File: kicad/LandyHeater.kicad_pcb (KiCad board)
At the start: 4 copper layers, 0 parts

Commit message: Place Rev B board: outline, zoned placement, mounting holes, V-01 transient check
- 80 x 50 mm outline, all 131 parts on the top side, 4 x M3 board-only holes
- Custom DRC rules: 0.2 mm general clearance with justified exceptions for
  fine-pitch IC pads, the USB pair and the USB-C guide pins; 0.2 mm min drill
- ngspice transient check of the 12 V input (ISO 7637-2 level IV pulses)
- Phase 3 report for approval

Co-Authored-By: Claude Opus 5.5 <noreply@anthropic.com>
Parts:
- added BT1: BR1225, LandyHeater:BatteryClip_MYOUNG_MY-1225-01-J, F.Cu at (129.0, 108.0)
- added C1: 47uF, Capacitor_SMD:CP_Elec_6.3x7.7, F.Cu at (117.7, 132.0)
- added C10: 22uF, Capacitor_SMD:C_1206_3216Metric, F.Cu at (120.0, 119.5)
- added C11: 22uF, Capacitor_SMD:C_1206_3216Metric, F.Cu at (120.0, 124.2)
- added C12: 22uF, Capacitor_SMD:C_1206_3216Metric, F.Cu at (147.6, 102.9)
- added C13: 22uF, Capacitor_SMD:C_1206_3216Metric, F.Cu at (150.3, 102.9)
- added C14: 100nF, Capacitor_SMD:C_0603_1608Metric, F.Cu at (147.2, 107.1)
- added C15: 1uF, Capacitor_SMD:C_0603_1608Metric, F.Cu at (145.3, 102.1)
- added C16: 100nF, Capacitor_SMD:C_0603_1608Metric, F.Cu at (149.8, 119.7)
- added C17: 10pF, Capacitor_SMD:C_0603_1608Metric, F.Cu at (153.0, 129.4)
- added C18: 10pF, Capacitor_SMD:C_0603_1608Metric, F.Cu at (166.1, 130.9)
- added C19: 100nF, Capacitor_SMD:C_0603_1608Metric, F.Cu at (131.0, 116.4)
- added C2: 1uF, Capacitor_SMD:C_0603_1608Metric, F.Cu at (160.6, 124.2)
- added C20: 1uF, Capacitor_SMD:C_0603_1608Metric, F.Cu at (129.3, 123.8)
- added C21: 100nF, Capacitor_SMD:C_0603_1608Metric, F.Cu at (126.4, 125.7)
- added C22: 100nF, Capacitor_SMD:C_0603_1608Metric, F.Cu at (123.0, 125.7)
- added C23: 1uF, Capacitor_SMD:C_0603_1608Metric, F.Cu at (149.6, 127.9)
- added C24: 1uF, Capacitor_SMD:C_0603_1608Metric, F.Cu at (142.0, 128.3)
- added C25: 10nF, Capacitor_SMD:C_0603_1608Metric, F.Cu at (134.1, 128.3)
- added C3: 10nF, Capacitor_SMD:C_0603_1608Metric, F.Cu at (166.3, 127.5)
- added C4: 1nF, Capacitor_SMD:C_0603_1608Metric, F.Cu at (154.9, 127.6)
- added C5: 4.7uF, Capacitor_SMD:C_0603_1608Metric, F.Cu at (156.8, 127.6)
- added C6: 4.7uF, Capacitor_SMD:C_1206_3216Metric, F.Cu at (104.5, 121.5)
- added C7: 100nF, Capacitor_SMD:C_0603_1608Metric, F.Cu at (107.0, 121.5)
- added C8: 1uF, Capacitor_SMD:C_0603_1608Metric, F.Cu at (110.0, 125.0)
- added C9: 100nF, Capacitor_SMD:C_0603_1608Metric, F.Cu at (113.5, 117.5)
- added D1: SMBJ18CA, Diode_SMD:D_SMB, F.Cu at (103.5, 131.5)
- added D10: PESD3V3S2UT, Package_TO_SOT_SMD:SOT-23, F.Cu at (135.3, 124.7)
- added D11: rot, LED_SMD:LED_0603_1608Metric, F.Cu at (109.2, 101.4)
- added D12: rot, LED_SMD:LED_0603_1608Metric, F.Cu at (112.6, 101.4)
- added D13: rot, LED_SMD:LED_0603_1608Metric, F.Cu at (116.0, 101.4)
- added D14: rot, LED_SMD:LED_0603_1608Metric, F.Cu at (112.6, 103.3)
- added D15: BAS116, Package_TO_SOT_SMD:SOT-23, F.Cu at (115.5, 108.2)
- added D16: BAS116, Package_TO_SOT_SMD:SOT-23, F.Cu at (109.7, 109.0)
- added D17: BAS116, Package_TO_SOT_SMD:SOT-23, F.Cu at (102.6, 109.4)
- added D18: BAS116, Package_TO_SOT_SMD:SOT-23, F.Cu at (114.0, 112.0)
- added D19: rot, LED_SMD:LED_0603_1608Metric, F.Cu at (109.2, 103.3)
- added D2: SS16, Diode_SMD:D_SMA, F.Cu at (108.5, 131.5)
- added D20: rot, LED_SMD:LED_0603_1608Metric, F.Cu at (145.9, 116.3)
- added D21: rot, LED_SMD:LED_0603_1608Metric, F.Cu at (147.8, 116.3)
- added D3: ESD5Z5.0, Diode_SMD:D_SOD-523, F.Cu at (158.7, 124.0)
- added D4: SS16, Diode_SMD:D_SMA, F.Cu at (161.4, 131.2)
- added D5: BAS116, Package_TO_SOT_SMD:SOT-23, F.Cu at (134.1, 116.6)
- added D6: BAS116, Package_TO_SOT_SMD:SOT-23, F.Cu at (138.4, 119.9)
- added D7: ESD5Z5.0, Diode_SMD:D_SOD-523, F.Cu at (122.8, 123.7)
- added D8: PESD5V2S2UT, Package_TO_SOT_SMD:SOT-23, F.Cu at (123.6, 131.4)
- added D9: PESD3V3S2UT, Package_TO_SOT_SMD:SOT-23, F.Cu at (143.2, 124.7)
- added F1: 50mA, Fuse:Fuse_0805_2012Metric, F.Cu at (136.2, 128.5)
- added FB1: 600R, Inductor_SMD:L_0805_2012Metric, F.Cu at (112.5, 133.0)
- added H1: M3, MountingHole_3.2mm_M3, F.Cu at (104.0, 104.0)
- added H2: M3, MountingHole_3.2mm_M3, F.Cu at (176.0, 104.0)
- added H3: M3, MountingHole_3.2mm_M3, F.Cu at (104.0, 146.0)
- added H4: M3, MountingHole_3.2mm_M3, F.Cu at (176.0, 146.0)
- added J1: 12V IN, Connector_Molex:Molex_Nano-Fit_105313-xx02_1x02_P2.50mm_Horizontal, F.Cu at (113.0, 139.1)
- added J2: AUTOTERM, Connector_Molex:Molex_Nano-Fit_105313-xx04_1x04_P2.50mm_Horizontal, F.Cu at (129.0, 139.1)
- added J3: 1-Wire, Connector_Molex:Molex_Nano-Fit_105313-xx03_1x03_P2.50mm_Horizontal, F.Cu at (148.0, 139.1)
- added J4: Taster/LED, Connector_Molex:Molex_Nano-Fit_105313-xx05_1x05_P2.50mm_Horizontal, F.Cu at (164.0, 139.1)
- added J5: USB4105-GF-A-060, Connector_USB:USB_C_Receptacle_GCT_USB4105-xx-A_16P_TopMnt_Horizontal, F.Cu at (175.8, 128.0)
- added L1: 2.2uH, LandyHeater:L_CJiang_FAUL0420, F.Cu at (115.5, 121.5)
- added Q1: 2N7002K, Package_TO_SOT_SMD:SOT-23, F.Cu at (118.3, 112.0)
- added R1: 5.1k, Resistor_SMD:R_0603_1608Metric, F.Cu at (155.0, 124.2)
- added R10: 22R, Resistor_SMD:R_0603_1608Metric, F.Cu at (168.9, 128.8)
- added R11: 499R, Resistor_SMD:R_0603_1608Metric, F.Cu at (122.4, 119.8)
- added R12: 4.7k, Resistor_SMD:R_0603_1608Metric, F.Cu at (128.1, 119.0)
- added R13: 4.7k, Resistor_SMD:R_0603_1608Metric, F.Cu at (141.5, 119.7)
- added R14: 100k, Resistor_SMD:R_0603_1608Metric, F.Cu at (143.4, 119.7)
- added R15: 100R, Resistor_SMD:R_0603_1608Metric, F.Cu at (125.9, 123.8)
- added R16: 100R, Resistor_SMD:R_0603_1608Metric, F.Cu at (123.1, 127.6)
- added R17: 1k, Resistor_SMD:R_0603_1608Metric, F.Cu at (126.5, 128.6)
- added R18: 100k, Resistor_SMD:R_0603_1608Metric, F.Cu at (129.9, 128.6)
- added R19: 100k, Resistor_SMD:R_0603_1608Metric, F.Cu at (143.9, 128.3)
- added R2: 5.1k, Resistor_SMD:R_0603_1608Metric, F.Cu at (156.9, 124.2)
- added R20: 4.7k, Resistor_SMD:R_0603_1608Metric, F.Cu at (149.7, 124.5)
- added R21: 0R, Resistor_SMD:R_0603_1608Metric, F.Cu at (147.0, 123.8)
- added R22: 1k, Resistor_SMD:R_0603_1608Metric, F.Cu at (138.4, 124.5)
- added R23: 10k, Resistor_SMD:R_0603_1608Metric, F.Cu at (138.4, 127.9)
- added R24: 100R, Resistor_SMD:R_0603_1608Metric, F.Cu at (138.5, 131.3)
- added R25: 100k, Resistor_SMD:R_0603_1608Metric, F.Cu at (138.5, 134.7)
- added R26: 12k, Resistor_SMD:R_0603_1608Metric, F.Cu at (118.6, 108.0)
- added R27: 3.3k, Resistor_SMD:R_0603_1608Metric, F.Cu at (105.7, 109.2)
- added R28: 1k, Resistor_SMD:R_0603_1608Metric, F.Cu at (138.3, 116.3)
- added R29: 3.3k, Resistor_SMD:R_0603_1608Metric, F.Cu at (140.2, 116.3)
- added R3: 100k, Resistor_SMD:R_0603_1608Metric, F.Cu at (168.7, 124.2)
- added R30: 1.8k, Resistor_SMD:R_0603_1608Metric, F.Cu at (142.1, 116.3)
- added R31: 100k, Resistor_SMD:R_0603_1608Metric, F.Cu at (144.0, 116.3)
- added R32: 1k, Resistor_SMD:R_0603_1608Metric, F.Cu at (149.7, 116.3)
- added R33: 1k, Resistor_SMD:R_0603_1608Metric, F.Cu at (122.4, 116.4)
- added R34: 100k, Resistor_SMD:R_0603_1608Metric, F.Cu at (124.3, 116.4)
- added R35: 100k, Resistor_SMD:R_0603_1608Metric, F.Cu at (126.2, 116.4)
- added R4: 10k, Resistor_SMD:R_0603_1608Metric, F.Cu at (153.0, 126.0)
- added R5: 28.7k, Resistor_SMD:R_0603_1608Metric, F.Cu at (162.5, 127.1)
- added R6: 3.32k, Resistor_SMD:R_0603_1608Metric, F.Cu at (164.4, 127.5)
- added R7: 10k, Resistor_SMD:R_0603_1608Metric, F.Cu at (143.4, 102.1)
- added R8: 10k, Resistor_SMD:R_0603_1608Metric, F.Cu at (143.4, 105.5)
- added R9: 22R, Resistor_SMD:R_0603_1608Metric, F.Cu at (168.9, 126.9)
- added SW1: RESET, Button_Switch_SMD:SW_Push_1P1T-SH_NO_CK_KMR2xxG, F.Cu at (140.4, 103.4)
- added SW2: BOOT, Button_Switch_SMD:SW_Push_1P1T-SH_NO_CK_KMR2xxG, F.Cu at (140.4, 109.4)
- added SW3: DIAG, Button_Switch_SMD:SW_Push_1P1T-SH_NO_CK_KMR2xxG, F.Cu at (117.3, 104.3)
- added TP1: BATT_12V_IN, TestPoint:TestPoint_Pad_D1.5mm, F.Cu at (102.3, 125.5)
- added TP10: U0TXD, TestPoint:TestPoint_Pad_D1.5mm, F.Cu at (124.8, 119.6)
- added TP11: U0RXD, TestPoint:TestPoint_Pad_D1.5mm, F.Cu at (130.5, 119.6)
- added TP12: I2C_SDA, TestPoint:TestPoint_Pad_D1.5mm, F.Cu at (142.5, 131.5)
- added TP13: I2C_SCL, TestPoint:TestPoint_Pad_D1.5mm, F.Cu at (145.4, 131.7)
- added TP14: RTC_INT_N, TestPoint:TestPoint_Pad_D1.5mm, F.Cu at (148.3, 134.0)
- added TP15: GND, TestPoint:TestPoint_Pad_D1.5mm, F.Cu at (155.4, 130.8)
- added TP16: AUTOTERM_5V, TestPoint:TestPoint_Pad_D1.5mm, F.Cu at (116.9, 125.5)
- added TP17: CTRL_TX, TestPoint:TestPoint_Pad_D1.5mm, F.Cu at (127.2, 131.0)
- added TP18: CTRL_RX, TestPoint:TestPoint_Pad_D1.5mm, F.Cu at (130.1, 131.0)
- added TP19: TX_3V3, TestPoint:TestPoint_Pad_D1.5mm, F.Cu at (127.2, 133.9)
- added TP2: 12V_PROT, TestPoint:TestPoint_Pad_D1.5mm, F.Cu at (112.5, 129.0)
- added TP20: RX_3V3, TestPoint:TestPoint_Pad_D1.5mm, F.Cu at (130.1, 133.9)
- added TP21: OE, TestPoint:TestPoint_Pad_D1.5mm, F.Cu at (122.9, 134.8)
- added TP22: 1WIRE_DQ_C, TestPoint:TestPoint_Pad_D1.5mm, F.Cu at (146.3, 128.8)
- added TP23: 3V3_SENSOR_SW, TestPoint:TestPoint_Pad_D1.5mm, F.Cu at (149.2, 131.1)
- added TP24: DIAG, TestPoint:TestPoint_Pad_D1.5mm, F.Cu at (109.0, 105.7)
- added TP25: GND, TestPoint:TestPoint_Pad_D1.5mm, F.Cu at (111.9, 105.7)
- added TP26: BUTTON_N, TestPoint:TestPoint_Pad_D1.5mm, F.Cu at (134.5, 135.7)
- added TP27: BUTTON_LED_PWM, TestPoint:TestPoint_Pad_D1.5mm, F.Cu at (149.6, 106.9)
- added TP28: DIAG_RUN, TestPoint:TestPoint_Pad_D1.5mm, F.Cu at (106.2, 112.4)
- added TP3: VIN_SYS, TestPoint:TestPoint_Pad_D1.5mm, F.Cu at (102.3, 116.0)
- added TP4: 3V3_CORE, TestPoint:TestPoint_Pad_D1.5mm, F.Cu at (117.0, 116.0)
- added TP5: USB_VBUS, TestPoint:TestPoint_Pad_D1.5mm, F.Cu at (163.0, 124.0)
- added TP6: VBUS_PROT, TestPoint:TestPoint_Pad_D1.5mm, F.Cu at (159.2, 127.4)
- added TP7: GND, TestPoint:TestPoint_Pad_D1.5mm, F.Cu at (106.0, 126.0)
- added TP8: EN, TestPoint:TestPoint_Pad_D1.5mm, F.Cu at (143.9, 108.7)
- added TP9: BOOT_N, TestPoint:TestPoint_Pad_D1.5mm, F.Cu at (143.9, 111.6)
- added U1: TPD2EUSB30DRTR, Package_TO_SOT_SMD:Texas_DRT-3, F.Cu at (153.0, 123.4)
- added U2: TPS259470LRPWR, LandyHeater:TI_RPW0010A_VQFN-HR-10_2x2mm, F.Cu at (166.1, 124.2)
- added U3: LMR43620MSC3RPERQ1, LandyHeater:TI_RPE0009A_VQFN-HR-9_2x2mm, F.Cu at (110.0, 121.5)
- added U4: ESP32-S3-WROOM-1U-N16R8, RF_Module:ESP32-S3-WROOM-1U, F.Cu at (162.0, 112.0)
- added U5: TPS3808G33DBVR, Package_TO_SOT_SMD:SOT-23-6, F.Cu at (146.6, 119.9)
- added U6: RV-8263-C8, LandyHeater:MicroCrystal_C8_SON-8_2.0x1.2mm, F.Cu at (128.6, 116.0)
- added U7: TXU0202QDCURQ1, Package_SO:VSSOP-8_2.3x2mm_P0.5mm, F.Cu at (130.6, 126.2)
- added U8: TPS22945DCKR, Package_TO_SOT_SMD:SOT-353_SC-70-5, F.Cu at (147.0, 126.0)
- added U9: BCR421UW6Q-7, Package_TO_SOT_SMD:SOT-23-6, F.Cu at (135.3, 132.3)
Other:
- board outline added: 80 x 50 mm

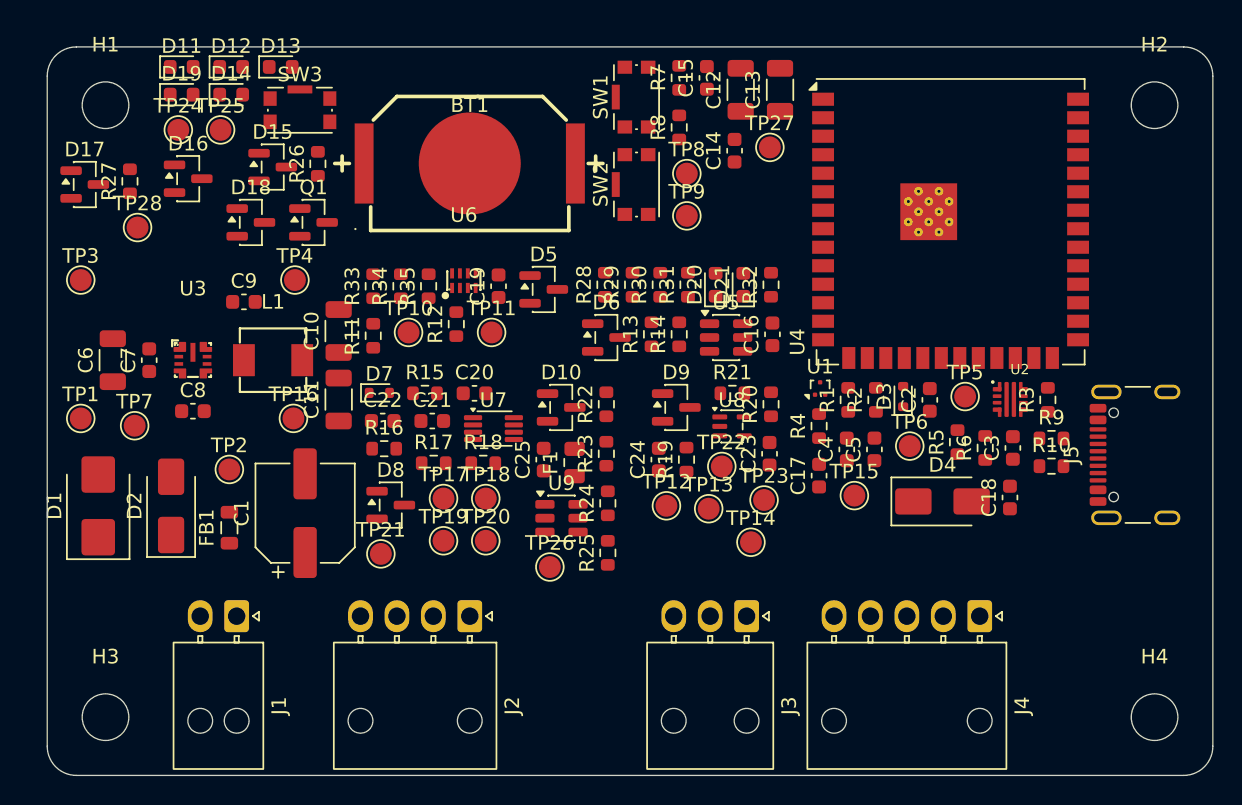
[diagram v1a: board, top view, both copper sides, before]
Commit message: Rework Rev B placement for short connections and layout checklist
- Reassign ESP32 GPIOs so each block sits at the module edge facing it
  (schematic, requirements A12 v2.1, firmware note P2-04)
- Connectivity-driven placement: decoupling within 2 mm of its pin, USB
  series resistors at the module, ESD parts at their connectors, diagnostic
  LEDs in one row; total connection length 1377 -> 729 mm
- Connector order J1, J2, J4, J3; three fiducials; Power net class 0.65 mm
- Layout checklist B7 from Espressif, TI, JLCPCB and EMC guidance

Co-Authored-By: Claude Opus 5.5 <noreply@anthropic.com>
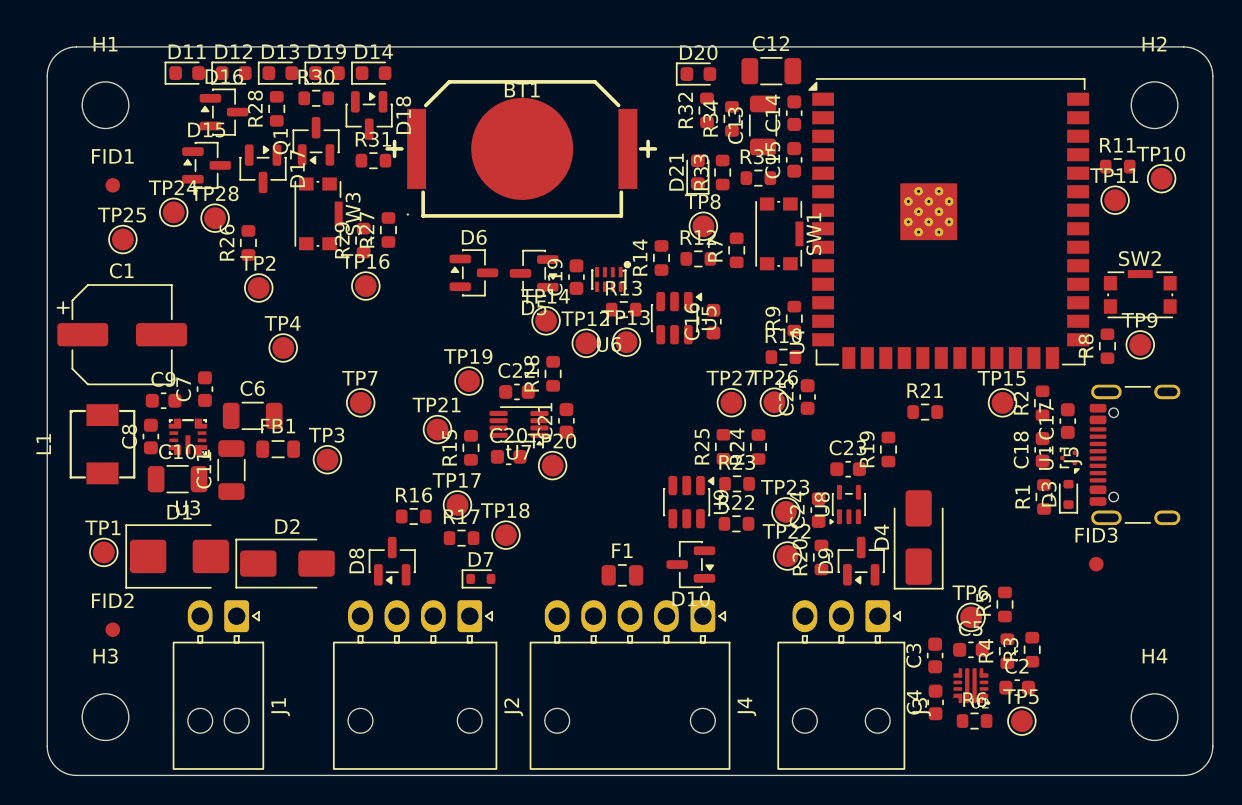
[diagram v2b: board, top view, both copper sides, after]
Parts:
- added FID1: Fiducial, Fiducial_1mm_Mask2mm, F.Cu at (104.5, 109.5)
- added FID2: Fiducial, Fiducial_1mm_Mask2mm, F.Cu at (104.5, 140.0)
- added FID3: Fiducial, Fiducial_1mm_Mask2mm, F.Cu at (172.0, 135.5)
- moved TP10 52.8 mm to (176.5, 109.0)
- moved R11 52.4 mm to (173.5, 108.2), turned to 0 degrees
- moved TP11 43.7 mm to (173.3, 110.5)
- moved SW2 35.4 mm to (175.0, 117.0), turned to 0 degrees
- moved R8 33.0 mm to (172.8, 120.5)
- moved TP9 32.4 mm to (175.0, 120.5)
- moved R30 26.9 mm to (118.5, 103.5), turned to 0 degrees
- moved R28 25.6 mm to (115.8, 104.3)
- moved R34 25.5 mm to (147.0, 104.9)
- moved R33 25.2 mm to (146.4, 108.6)
- moved R35 23.8 mm to (148.8, 109.0), turned to 0 degrees
- moved R31 23.2 mm to (122.4, 107.8), turned to 0 degrees
- moved TP5 22.6 mm to (166.9, 146.3)
- moved TP3 20.9 mm to (119.2, 128.3)
- moved TP14 20.7 mm to (134.2, 118.8)
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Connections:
- U4 pad 12: /ESP32 und RTC/I2C_SDA -> AUTOTERM_OE
- U4 pad 17: /ESP32 und RTC/I2C_SCL -> BUTTON_N
- U4 pad 18: DIAG_RUN -> BUTTON_LED_PWM
- U4 pad 19: STATUS_LED_1 -> unconnected-(U4-IO11-Pad19)
- U4 pad 20: STATUS_LED_2 -> unconnected-(U4-IO12-Pad20)
- U4 pad 21: unconnected-(U4-IO13-Pad21) -> 1WIRE_DQ
- U4 pad 22: unconnected-(U4-IO14-Pad22) -> SENSOR_EN
- U4 pad 38: /ESP32 und RTC/RTC_INT_N -> unconnected-(U4-IO2-Pad38)
- U4 pad 39: BUTTON_N -> unconnected-(U4-IO1-Pad39)
- U4 pad 4: 1WIRE_DQ -> STATUS_LED_1
- U4 pad 5: SENSOR_EN -> STATUS_LED_2
- U4 pad 6: AUTOTERM_OE -> DIAG_RUN
- U4 pad 7: BUTTON_LED_PWM -> /ESP32 und RTC/RTC_INT_N
- U4 pad 8: unconnected-(U4-IO15-Pad8) -> /ESP32 und RTC/I2C_SDA
- U4 pad 9: unconnected-(U4-IO16-Pad9) -> /ESP32 und RTC/I2C_SCL

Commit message: Add C26 100 nF at 12V_PROT ahead of the ferrite (E-01)
Forms a pi filter with FB1 and C1 and limits the reverse voltage across D2
in ISO 7637-2 pulse 3a from 60.3 V to 38.8 V (SPICE, sim/v01_transienten.py).
Placed between D2 and FB1; ERC, netlist check and DRC clean.

Co-Authored-By: Claude Opus 5.5 <noreply@anthropic.com>
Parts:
- added C26: 100nF, Capacitor_SMD:C_0603_1608Metric, F.Cu at (115.4, 132.4)
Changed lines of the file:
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@@
 		(embedded_fonts no)
+	)
+	(footprint "Capacitor_SMD:C_0603_1608Metric"
+		(layer "F.Cu")
+		(at 115.4 132.4)
+		(descr "Capacitor SMD 0603 (1608 Metric), square (rectangular) end terminal, IPC-7351 nominal, (Body size source: IPC-SM-782 page 76, https://www.pcb-3d.com/wordpress/wp-content/uploads/ipc-sm-782a_amendment_1_and_2.pdf)")
+		(tags "capacitor")
+		(property "Reference" "C26"
+			(at 0 -1.43 0)
+			(layer "F.SilkS")
+			(effects
+				(font
+					(size 1 1)
+					(thickness 0.15)
+				)
+			)
+		)
+		(property "Value" "100nF"
+			(at 0 1.43 0)
+			(layer "F.Fab")
+			(effects
+				(font
+					(size 1 1)
+					(thickness 0.15)
+				)
+			)
+		)
+		(property "Datasheet" ""
+			(at 0 0 0)
+			(layer "F.Fab")
+			(hide yes)
+			(effects
+				(font
+					(size 1.27 1.27)
+				)
+			)
+		)
+		(property "Description" "Unpolarized capacitor"
+			(at 0 0 0)
+			(layer "F.Fab")
+			(hide yes)
+			(effects
+				(font
+					(size 1.27 1.27)
+				)
+			)
+		)
+		(property "KiLib_Generator" "SMD_2terminal_chip_molded"
+			(at 0 0 0)
+			(layer "F.SilkS")
+			(hide yes)
+			(effects
+				(font
+					(size 1 1)
+					(thickness 0.15)
+				)
+			)
+		)
+		(property "Spez" "X7R 50 V 0603"
+			(at 0 0 0)
+			(layer "F.SilkS")
+			(hide yes)
+			(effects
+				(font
+					(size 1.27 1.27)
+					(thickness 0.15)
+				)
+			)
+		)
+		(sheetname "/Versorgung/")
+		(sheetfile "01_Versorgung.kicad_sch")
+		(attr smd)
+		(duplicate_pad_numbers_are_jumpers no)
+		(fp_line
+			(start -0.14058 -0.51)
+			(end 0.14058 -0.51)
+			(stroke
+				(width 0.12)
+				(type solid)
+			)
+			(layer "F.SilkS")
+		)
+		(fp_line
+			(start -0.14058 0.51)
+			(end 0.14058 0.51)
+			(stroke
+				(width 0.12)
+				(type solid)
+			)
+			(layer "F.SilkS")
+		)
+		(fp_rect
+			(start -1.48 -0.73)
+			(end 1.48 0.73)
+			(stroke
+				(width 0.05)
+				(type solid)
+			)
+			(fill no)
+			(layer "F.CrtYd")
+		)
+		(fp_rect
+			(start -0.8 -0.4)
+			(end 0.8 0.4)
+			(stroke
+				(width 0.1)
+				(type solid)
+			)
+			(fill no)
+			(layer "F.Fab")
+		)
+		(fp_text user "${REFERENCE}"
+			(at 0 0 0)
+			(layer "F.Fab")
+			(effects
+				(font
+					(size 0.4 0.4)
+					(thickness 0.06)
+				)
+			)
+		)
+		(pad "1" smd roundrect
+			(at -0.775 0)
+			(size 0.9 0.95)
+			(layers "F.Cu" "F.Mask" "F.Paste")
+			(roundrect_rratio 0.25)
+			(net "12V_PROT")
+		)
+		(pad "2" smd roundrect
+			(at 0.775 0)
+			(size 0.9 0.95)
+			(layers "F.Cu" "F.Mask" "F.Paste")
+			(roundrect_rratio 0.25)
+			(net "GND")
+		)
+		(embedded_fonts no)
+		(model "${KICAD10_3DMODEL_DIR}/Capacitor_SMD.3dshapes/C_0603_1608Metric.step"
+			(offset
+				(xyz 0 0 0)
+			)
+			(scale
+				(xyz 1 1 1)
+			)
+			(rotate
+				(xyz 0 0 0)
+			)
+		)
 	)
 	(footprint "Package_TO_SOT_SMD:SOT-23"

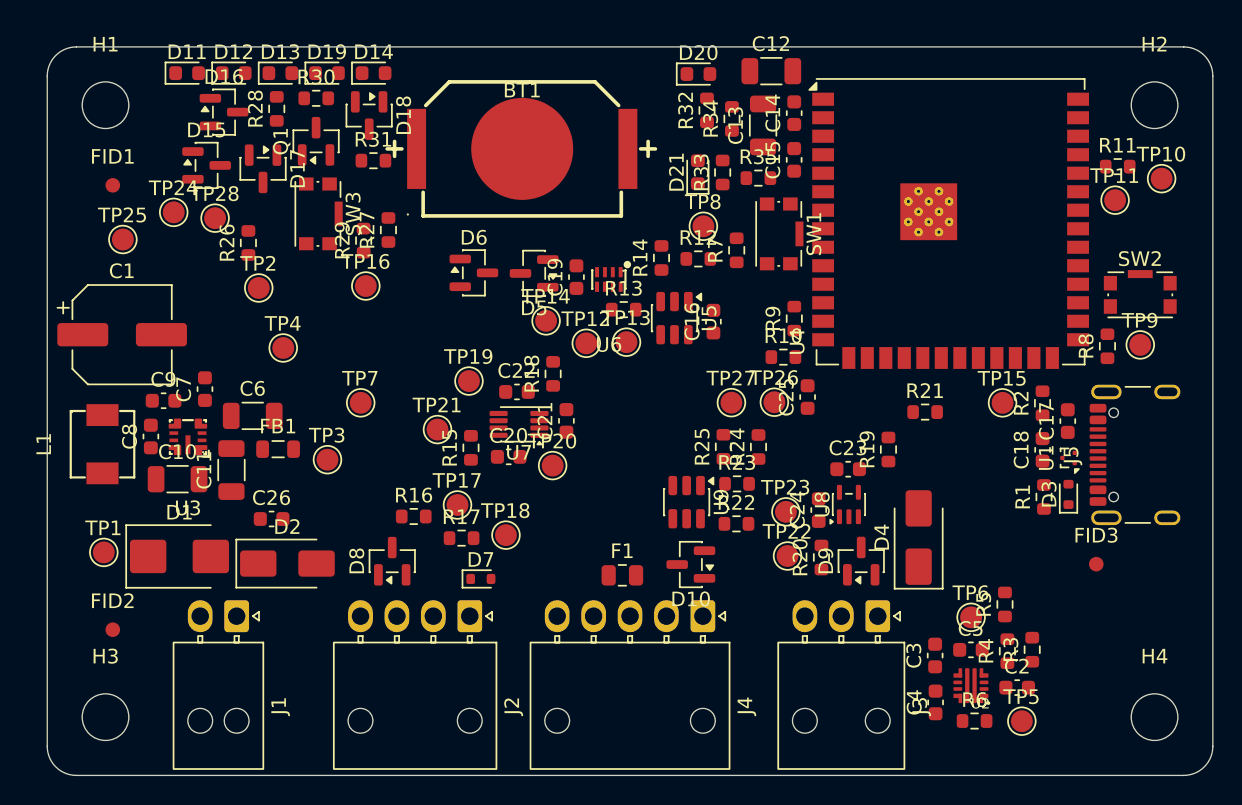
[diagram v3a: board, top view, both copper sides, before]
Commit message: Placement milestone steps 3-5: hierarchical placement and validation
- tools/place_v2.py: all 139 positions explicit and justified per block,
  following the approved floorplan and datasheet layout guidance
- tools/check_placement.py: datasheet distances, SW-node separation,
  courtyards, hole clearance, routing corridors (fan-out, USB pair)
- tools/ratsnest_metrics.py, tools/update_footprints.py (1 nm rounding
  mismatches resolved; pads, nets, fields verified unchanged)
- RESET and BOOT side by side on the right edge to free the module fan-out
- Placement report with renders, decisions, DRC classification, positions

Co-Authored-By: Claude Opus 5.5 <noreply@anthropic.com>
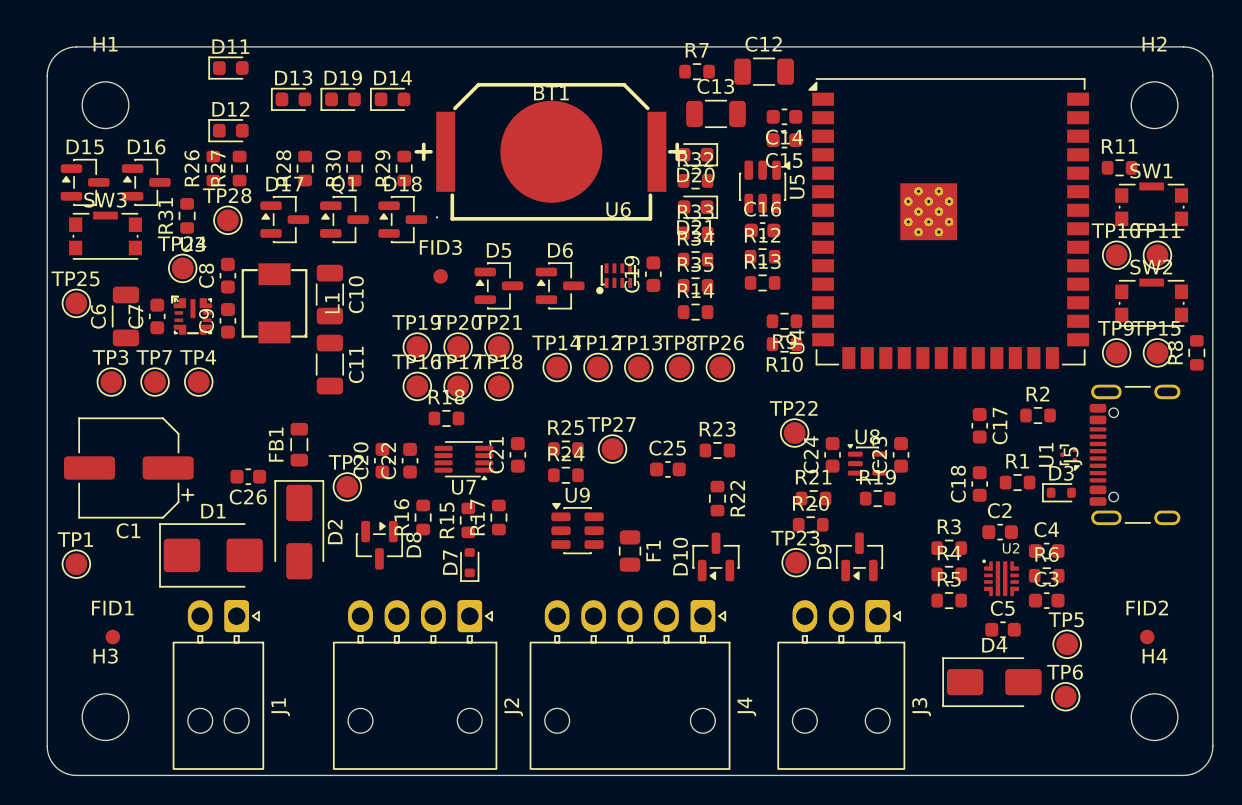
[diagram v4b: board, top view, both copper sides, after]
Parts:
- moved FID2 71.0 mm to (175.5, 140.5)
- moved FID3 49.1 mm to (127.0, 115.8)
- moved FID1 31.0 mm to (104.5, 140.5)
- moved SW1 25.7 mm to (175.8, 111.0), turned to 0 degrees
- moved C10 16.4 mm to (119.4, 117.0), turned to -90 degrees
- moved TP3 15.8 mm to (104.4, 123.0)
- moved L1 15.3 mm to (115.6, 117.6), turned to -90 degrees
- moved TP2 14.9 mm to (120.6, 130.2)
- moved SW3 14.7 mm to (104.0, 113.0), turned to 0 degrees
- moved TP7 14.2 mm to (107.4, 123.0)
- moved R24 13.4 mm to (135.6, 129.4), turned to 0 degrees
- moved R31 13.3 mm to (109.6, 111.6), turned to 90 degrees
- moved C4 12.9 mm to (168.6, 134.6), turned to 0 degrees
- moved R7 12.6 mm to (144.6, 101.7), turned to 0 degrees
- moved C8 12.2 mm to (112.4, 115.7)
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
